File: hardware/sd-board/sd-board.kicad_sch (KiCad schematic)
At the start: 9 parts, among them J1 TF-01A push-push, P1 to the FM-1, U1 74LVC1G04

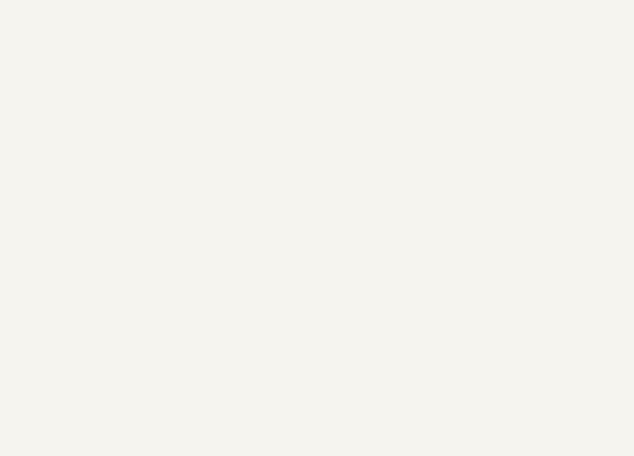
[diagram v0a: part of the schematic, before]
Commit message: feat(hardware): the SD board 26 x 36 mm (the 27 x 40 mm free beside the FM-1's battery) with four 2.2 mm holes in its corners (M2 screw, zip tie, rivet: the user's 'to easily attach it to something'), in the schematic too; DRC 0 errors, nets 0 differ
Co-Authored-By: Claude Opus 5.5 <noreply@anthropic.com>
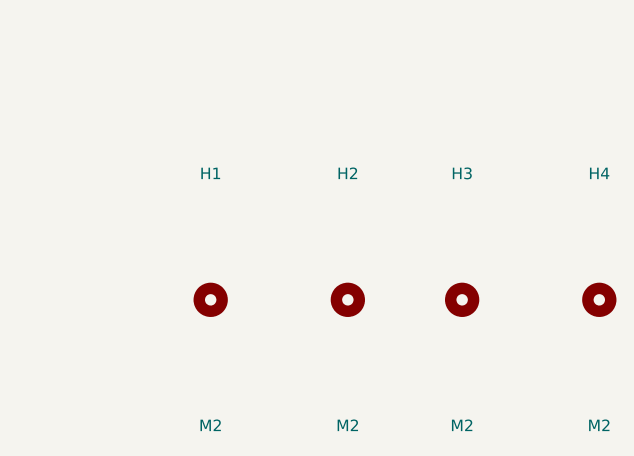
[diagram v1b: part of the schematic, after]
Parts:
- added H1, H2, H3, H4: M2, MountingHole:MountingHole_2.2mm_M2, symbol Mechanical:MountingHole
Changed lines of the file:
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@@
 (label "MISO" (at 226.06 96.52 180) (effects (font (size 1.27 1.27)) (justify right bottom)))
 (no_connect (at 226.06 83.82))
+(symbol (lib_id "Mechanical:MountingHole") (at 215.9 149.86 0) (unit 1) (exclude_from_sim no) (in_bom no) (on_board yes) (dnp no) (property "Reference" "H1" (at 215.9 135.86 0) (effects (font (size 1.27 1.27)))) (property "Value" "M2" (at 215.9 163.86 0) (effects (font (size 1.27 1.27)))) (property "Footprint" "MountingHole:MountingHole_2.2mm_M2" (at 215.9 149.86 0) (effects (font (size 1.27 1.27)) (hide yes))) (property "Datasheet" "" (at 215.9 149.86 0) (effects (font (size 1.27 1.27)) (hide yes))) (property "LCSC" "" (at 215.9 149.86 0) (effects (font (size 1.27 1.27)) (hide yes)))  (instances (project "sd-board" (path "/766c70bd-1acb-59f5-b703-96c0315a8041" (reference "H1") (unit 1)))))
+(symbol (lib_id "Mechanical:MountingHole") (at 231.14 149.86 0) (unit 1) (exclude_from_sim no) (in_bom no) (on_board yes) (dnp no) (property "Reference" "H2" (at 231.14 135.86 0) (effects (font (size 1.27 1.27)))) (property "Value" "M2" (at 231.14 163.86 0) (effects (font (size 1.27 1.27)))) (property "Footprint" "MountingHole:MountingHole_2.2mm_M2" (at 231.14 149.86 0) (effects (font (size 1.27 1.27)) (hide yes))) (property "Datasheet" "" (at 231.14 149.86 0) (effects (font (size 1.27 1.27)) (hide yes))) (property "LCSC" "" (at 231.14 149.86 0) (effects (font (size 1.27 1.27)) (hide yes)))  (instances (project "sd-board" (path "/766c70bd-1acb-59f5-b703-96c0315a8041" (reference "H2") (unit 1)))))
+(symbol (lib_id "Mechanical:MountingHole") (at 243.84 149.86 0) (unit 1) (exclude_from_sim no) (in_bom no) (on_board yes) (dnp no) (property "Reference" "H3" (at 243.84 135.86 0) (effects (font (size 1.27 1.27)))) (property "Value" "M2" (at 243.84 163.86 0) (effects (font (size 1.27 1.27)))) (property "Footprint" "MountingHole:MountingHole_2.2mm_M2" (at 243.84 149.86 0) (effects (font (size 1.27 1.27)) (hide yes))) (property "Datasheet" "" (at 243.84 149.86 0) (effects (font (size 1.27 1.27)) (hide yes))) (property "LCSC" "" (at 243.84 149.86 0) (effects (font (size 1.27 1.27)) (hide yes)))  (instances (project "sd-board" (path "/766c70bd-1acb-59f5-b703-96c0315a8041" (reference "H3") (unit 1)))))
+(symbol (lib_id "Mechanical:MountingHole") (at 259.08 149.86 0) (unit 1) (exclude_from_sim no) (in_bom no) (on_board yes) (dnp no) (property "Reference" "H4" (at 259.08 135.86 0) (effects (font (size 1.27 1.27)))) (property "Value" "M2" (at 259.08 163.86 0) (effects (font (size 1.27 1.27)))) (property "Footprint" "MountingHole:MountingHole_2.2mm_M2" (at 259.08 149.86 0) (effects (font (size 1.27 1.27)) (hide yes))) (property "Datasheet" "" (at 259.08 149.86 0) (effects (font (size 1.27 1.27)) (hide yes))) (property "LCSC" "" (at 259.08 149.86 0) (effects (font (size 1.27 1.27)) (hide yes)))  (instances (project "sd-board" (path "/766c70bd-1acb-59f5-b703-96c0315a8041" (reference "H4") (unit 1)))))
 (symbol (lib_id "power:PWR_FLAG") (at 40.64 149.86 0) (unit 1) (exclude_from_sim no) (in_bom no) (on_board no) (dnp no) (property "Reference" "#FLG01" (at 40.64 135.86 0) (effects (font (size 1.27 1.27)) (hide yes))) (property "Value" "PWR_FLAG" (at 40.64 163.86 0) (effects (font (size 1.27 1.27)) (hide yes))) (property "Footprint" "" (at 40.64 149.86 0) (effects (font (size 1.27 1.27)) (hide yes))) (property "Datasheet" "" (at 40.64 149.86 0) (effects (font (size 1.27 1.27)) (hide yes))) (property "LCSC" "" (at 40.64 149.86 0) (effects (font (size 1.27 1.27)) (hide yes))) (pin "1") (instances (project "sd-board" (path "/766c70bd-1acb-59f5-b703-96c0315a8041" (reference "#FLG01") (unit 1)))))
 (label "3V3" (at 40.64 149.86 0) (effects (font (size 1.27 1.27)) (justify left bottom)))

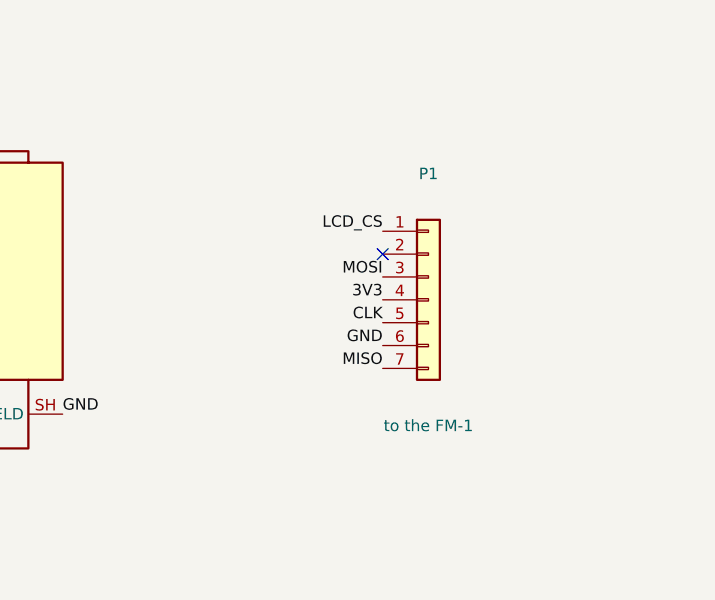
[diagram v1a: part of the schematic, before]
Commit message: feat(hardware): the SD board v2 for the back of the FM-1 (20 x 45.5 mm, the 20 x 60 free above the battery): a 6-pin 0.5 mm FFC socket (XUNPU FPC-05F-6PH20, C2856796) instead of the solder pads, for a flat cable from a tap at J12 around the board's edge (no soldering: the user); the card socket set back 5.5 mm, two holes beside its opening, two beside the FFC socket; the signals step from the card's 1.1 mm to the FFC's 0.5 mm pitch one at a time; the top pour's islands stitched; the schematic with Conn_01x06_MountingPin; DRC 0, nets 0 differ. The tap board at J12 is still to come (it needs J12's pin order)
Co-Authored-By: Claude Opus 5.5 <noreply@anthropic.com>
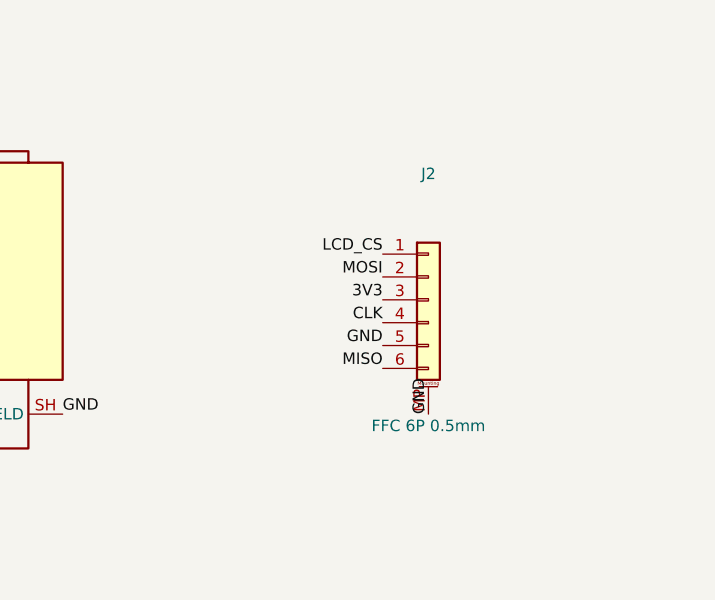
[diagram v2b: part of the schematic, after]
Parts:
- removed P1: to the FM-1, Connector_PinHeader_2.54mm:PinHeader_1x07_P2.54mm_Vertical, symbol Connector_Generic:Conn_01x07
- added J2: FFC 6P 0.5mm, sdboard:FPC-SMD_6P-P0.50_XUNPU_FPC-05F-6PH20, symbol Connector_Generic_MountingPin:Conn_01x06_MountingPin
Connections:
- net 3V3: now also J2.3 (Pin_3)
- net CLK: now also J2.4 (Pin_4)
- net GND: now also J2.5 (Pin_5), J2.MP (MountPin)
- net LCD_CS: now also J2.1 (Pin_1)
- net MISO: now also J2.6 (Pin_6)
- net MOSI: now also J2.2 (Pin_2)
- no-connect marks 3 -> 2
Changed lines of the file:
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@@
 (label "GND" (at 76.2 120.65 90) (effects (font (size 1.27 1.27)) (justify left bottom)))
 (label "3V3" (at 76.2 128.27 270) (effects (font (size 1.27 1.27)) (justify left bottom)))
-(symbol (lib_id "Connector_Generic:Conn_01x07") (at 231.14 88.9 0) (unit 1) (exclude_from_sim no) (in_bom no) (on_board yes) (dnp no) (property "Reference" "P1" (at 231.14 74.9 0) (effects (font (size 1.27 1.27)))) (property "Value" "to the FM-1" (at 231.14 102.9 0) (effects (font (size 1.27 1.27)))) (property "Footprint" "Connector_PinHeader_2.54mm:PinHeader_1x07_P2.54mm_Vertical" (at 231.14 88.9 0) (effects (font (size 1.27 1.27)) (hide yes))) (property "Datasheet" "" (at 231.14 88.9 0) (effects (font (size 1.27 1.27)) (hide yes))) (property "LCSC" "" (at 231.14 88.9 0) (effects (font (size 1.27 1.27)) (hide yes))) (pin "1") (pin "2") (pin "3") (pin "4") (pin "5") (pin "6") (pin "7") (instances (project "sd-board" (path "/766c70bd-1acb-59f5-b703-96c0315a8041" (reference "P1") (unit 1)))))
-(label "LCD_CS" (at 226.06 81.28 180) (effects (font (size 1.27 1.27)) (justify right bottom)))
+(symbol (lib_id "Connector_Generic_MountingPin:Conn_01x06_MountingPin") (at 231.14 88.9 0) (unit 1) (exclude_from_sim no) (in_bom yes) (on_board yes) (dnp no) (property "Reference" "J2" (at 231.14 74.9 0) (effects (font (size 1.27 1.27)))) (property "Value" "FFC 6P 0.5mm" (at 231.14 102.9 0) (effects (font (size 1.27 1.27)))) (property "Footprint" "sdboard:FPC-SMD_6P-P0.50_XUNPU_FPC-05F-6PH20" (at 231.14 88.9 0) (effects (font (size 1.27 1.27)) (hide yes))) (property "Datasheet" "" (at 231.14 88.9 0) (effects (font (size 1.27 1.27)) (hide yes))) (property "LCSC" "C2856796" (at 231.14 88.9 0) (effects (font (size 1.27 1.27)) (hide yes))) (pin "1") (pin "2") (pin "3") (pin "4") (pin "5") (pin "6") (pin "MP") (instances (project "sd-board" (path "/766c70bd-1acb-59f5-b703-96c0315a8041" (reference "J2") (unit 1)))))
+(label "LCD_CS" (at 226.06 83.82 180) (effects (font (size 1.27 1.27)) (justify right bottom)))
 (label "MOSI" (at 226.06 86.36 180) (effects (font (size 1.27 1.27)) (justify right bottom)))
 (label "3V3" (at 226.06 88.9 180) (effects (font (size 1.27 1.27)) (justify right bottom)))
@@
 (label "GND" (at 226.06 93.98 180) (effects (font (size 1.27 1.27)) (justify right bottom)))
 (label "MISO" (at 226.06 96.52 180) (effects (font (size 1.27 1.27)) (justify right bottom)))
-(no_connect (at 226.06 83.82))
+(label "GND" (at 231.14 101.6 270) (effects (font (size 1.27 1.27)) (justify left bottom)))
 (symbol (lib_id "Mechanical:MountingHole") (at 215.9 149.86 0) (unit 1) (exclude_from_sim no) (in_bom no) (on_board yes) (dnp no) (property "Reference" "H1" (at 215.9 135.86 0) (effects (font (size 1.27 1.27)))) (property "Value" "M2" (at 215.9 163.86 0) (effects (font (size 1.27 1.27)))) (property "Footprint" "MountingHole:MountingHole_2.2mm_M2" (at 215.9 149.86 0) (effects (font (size 1.27 1.27)) (hide yes))) (property "Datasheet" "" (at 215.9 149.86 0) (effects (font (size 1.27 1.27)) (hide yes))) (property "LCSC" "" (at 215.9 149.86 0) (effects (font (size 1.27 1.27)) (hide yes)))  (instances (project "sd-board" (path "/766c70bd-1acb-59f5-b703-96c0315a8041" (reference "H1") (unit 1)))))
 (symbol (lib_id "Mechanical:MountingHole") (at 231.14 149.86 0) (unit 1) (exclude_from_sim no) (in_bom no) (on_board yes) (dnp no) (property "Reference" "H2" (at 231.14 135.86 0) (effects (font (size 1.27 1.27)))) (property "Value" "M2" (at 231.14 163.86 0) (effects (font (size 1.27 1.27)))) (property "Footprint" "MountingHole:MountingHole_2.2mm_M2" (at 231.14 149.86 0) (effects (font (size 1.27 1.27)) (hide yes))) (property "Datasheet" "" (at 231.14 149.86 0) (effects (font (size 1.27 1.27)) (hide yes))) (property "LCSC" "" (at 231.14 149.86 0) (effects (font (size 1.27 1.27)) (hide yes)))  (instances (project "sd-board" (path "/766c70bd-1acb-59f5-b703-96c0315a8041" (reference "H2") (unit 1)))))
